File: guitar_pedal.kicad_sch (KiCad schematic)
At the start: 16 parts, among them J1 NMJ6HCD2, J2 NMJ6HCD2, J3 AVR-ISP-6, SW1 SW_SPST, U1 ATmega1284-P, U2 L7805, Y1 Crystal 16MHz

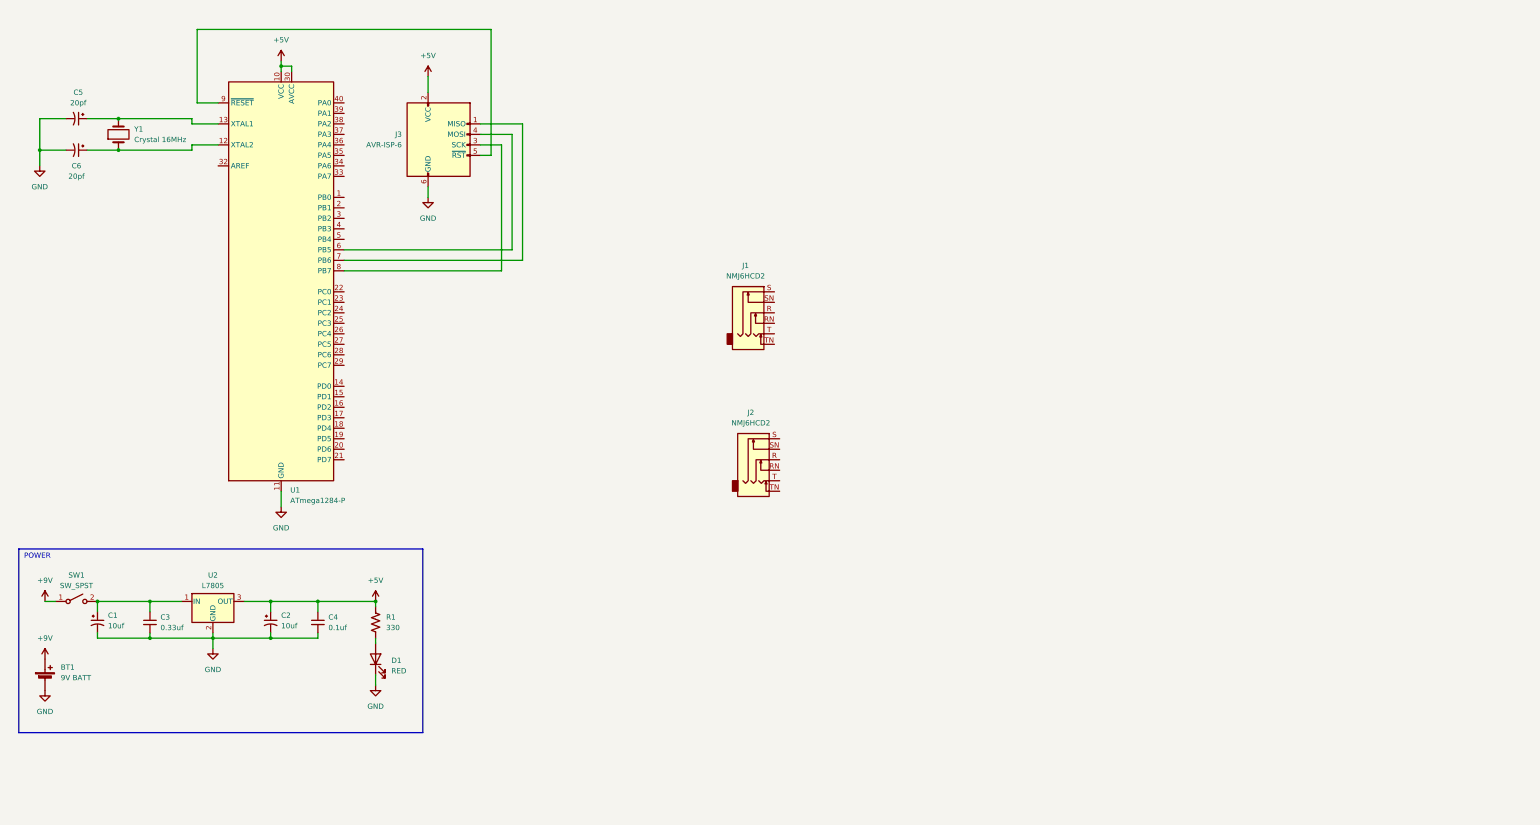
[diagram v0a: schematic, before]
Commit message: Added input/output op-amp buffer stages.
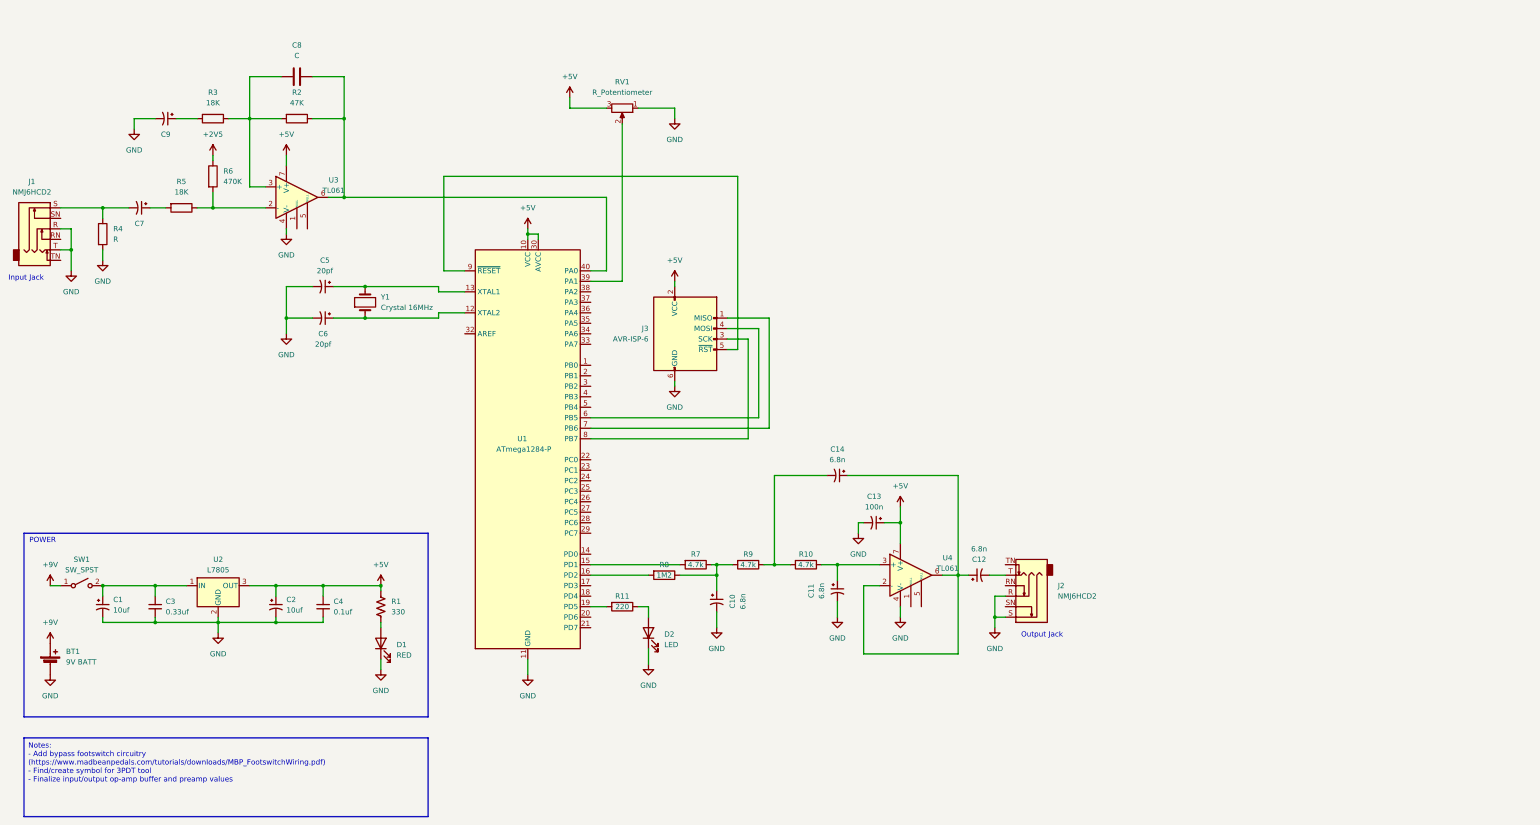
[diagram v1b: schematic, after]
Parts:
- added C10, C11, C12, C14: 6.8n, symbol Device:C_Polarized_Small_US
- added C13: 100n, symbol Device:C_Polarized_Small_US
- added C7, C9: ~, symbol Device:C_Polarized_Small_US
- added C8: C, symbol Device:C
- added D2: LED, symbol Device:LED
- added R10, R7, R9: 4.7k, symbol Device:R
- added R11: 220, symbol Device:R
- added R2: 47K, symbol Device:R
- added R3, R5: 18K, symbol Device:R
- added R4: R, symbol Device:R
- added R6: 470K, symbol Device:R
- added R8: 1M2, symbol Device:R
- added RV1: R_Potentiometer, symbol Device:R_Potentiometer
- added U3, U4: TL061, symbol Amplifier_Operational:TL061
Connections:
- net +5V: now also C13.1, RV1.3, U3.7 (V+), U4.7 (V+)
- net GND: now also J1.R, J1.T, J2.R, J2.S, C10.2, C11.2, C13.2, C9.2, D2.1 (K), R4.2, RV1.1, U3.4 (V-), U4.4 (V-)
- net at J2.T: now also C12.2
- net at U1.15 (PD1): now also R7.2
- net at U1.16 (PD2): now also R8.2
- net at U1.19 (PD5): now also R11.2
- net at U1.39 (PA1): now also RV1.2
- net at U1.40 (PA0): now also C8.2, R2.1, U3.6
- net at J1.S: now also C7.2, R4.1
- new net: C14.2, R10.2, R9.1
- new net: C10.1, R7.1, R8.1, R9.2
- new net: C12.1, C14.1, U4.2 (-), U4.6
- new net: C7.1, R5.2
- new net: D2.2 (A), R11.1
- new net: C11.1, R10.1, U4.3 (+)
- new net: C9.1, R3.2
- new net: R5.1, R6.2, U3.2 (-)
- new net: C8.1, R2.2, R3.1, U3.3 (+)
- new net +2V5: R6.1
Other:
- note added: "Input Jack"
- note added: "Output Jack"
- moved on the sheet: BT1, C1, C2, C3, C4, C5, C6, D1, J1, J2, J3, R1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

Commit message: Added bypass circuitry. Made edits to buffer stages + LED
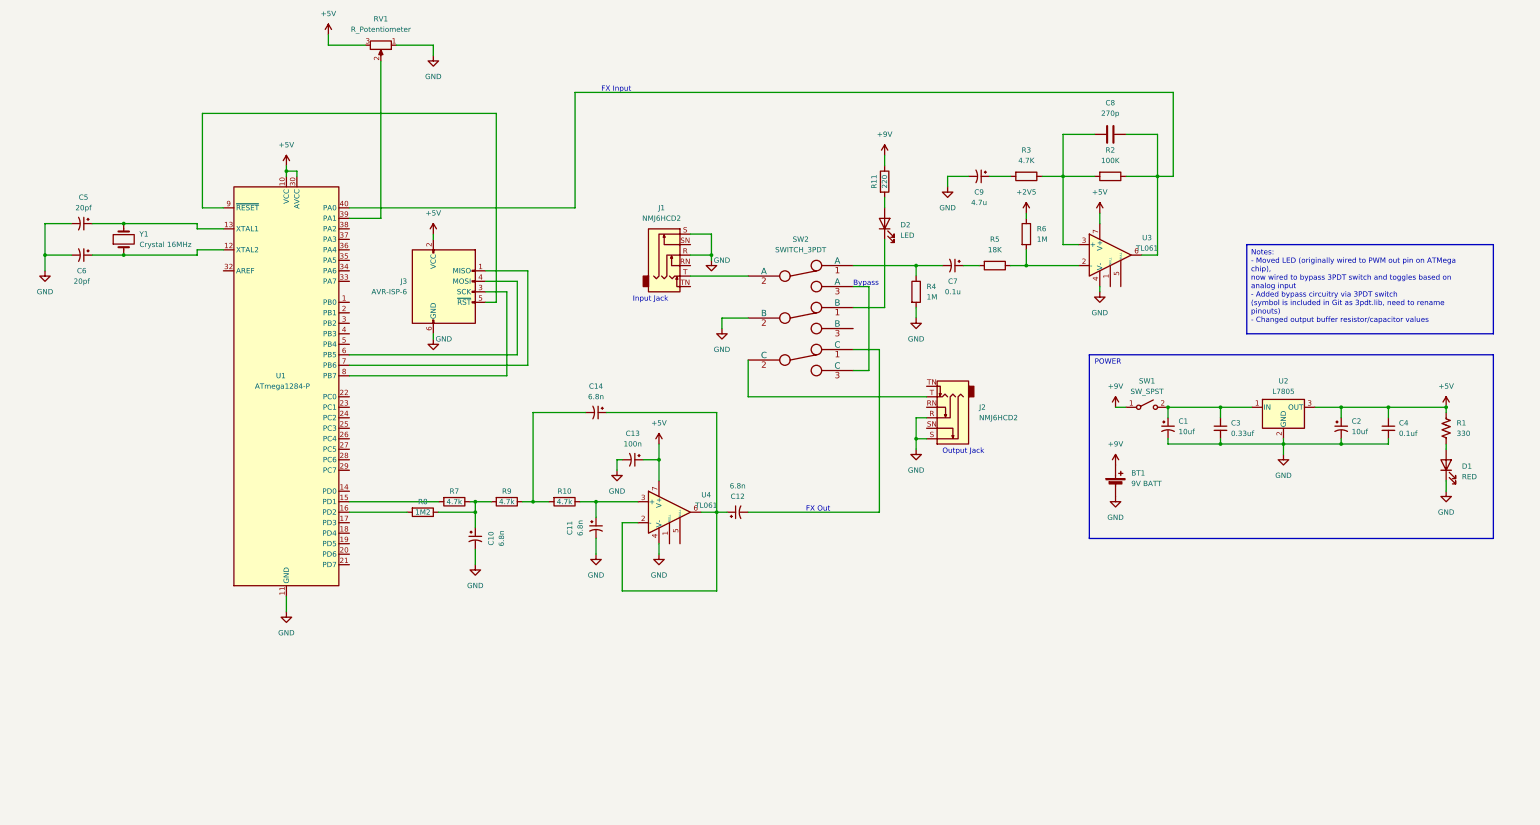
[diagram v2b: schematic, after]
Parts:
- added SW2: SWITCH_3PDT, symbol User:SWITCH_3PDT
- C7: value ~ -> 0.1u
- C8: value C -> 270p
- C9: value ~ -> 4.7u
- R2: value 47K -> 100K
- R3: value 18K -> 4.7K
- R4: value R -> 1M
- R6: value 470K -> 1M
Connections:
- net +9V: now also R11.1
- net GND: now also J1.S, SW2.2 (C); no longer D2.1 (K), J1.T
- net at C7.2, R4.1: now also SW2.1 (C); no longer J1.S
- net at D2.2 (A): now also R11.2; no longer R11.1
- net at U1.19 (PD5): no longer R11.2
- net at C12.2: now also SW2.1 (C); no longer J2.T
- new net: D2.1 (K), SW2.1 (C)
- new net: J2.T, SW2.2 (C)
- new net: J1.T, SW2.2 (C)
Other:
- note added: "Bypass"
- note added: "FX Input"
- note added: "FX Out"
- moved on the sheet: BT1, C1, C10, C11, C12, C13, C14, C2, C3, C4, C5, C6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
